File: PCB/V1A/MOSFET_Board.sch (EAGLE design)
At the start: 263 parts, among them IC301 7805T, IC302 7805T, J302 FAN_MOLEX4PIN, J303 FAN_MOLEX4PIN, Q201 SIRC10DP, Q202 SIRC10DP, Q203 BC817, Q204 BC817, Q205 SIRC10DP, Q206 SIRC10DP, Q207 BC817, Q208 BC807, Q209 BC817, Q210 BC807, Q211 IXTK102N65X2, Q212 IXTK102N65X2, Q401 BC807, Q402 BC807, Q403 BC807, Q404 BC807, Q405 BC807, Q406 BC807, Q407 BC807, Q408 BC807, Q409 BC807, Q410 BC807, Q411 BC807, Q412 BC807, Q413 BC807, Q414 BC807, U201 AD420, U202 AD420, U203 LT1014I, U204 LT1014I, U205 AD620, U206 AD620, U207 AD620, U208 AD620, U209 LTC1865L, U210 LTC1865L, U301 MAX743, U302 LP2985-3.1, U305 AD620, U306 LTC1865L, U307 LTC1865L, U401 HCPL-063N, U402 HCPL-063N, U403 HCPL-063N, U404 HCPL-063N, U405 HCPL-063N, U406 HCPL-063N, U407 HCPL-063N

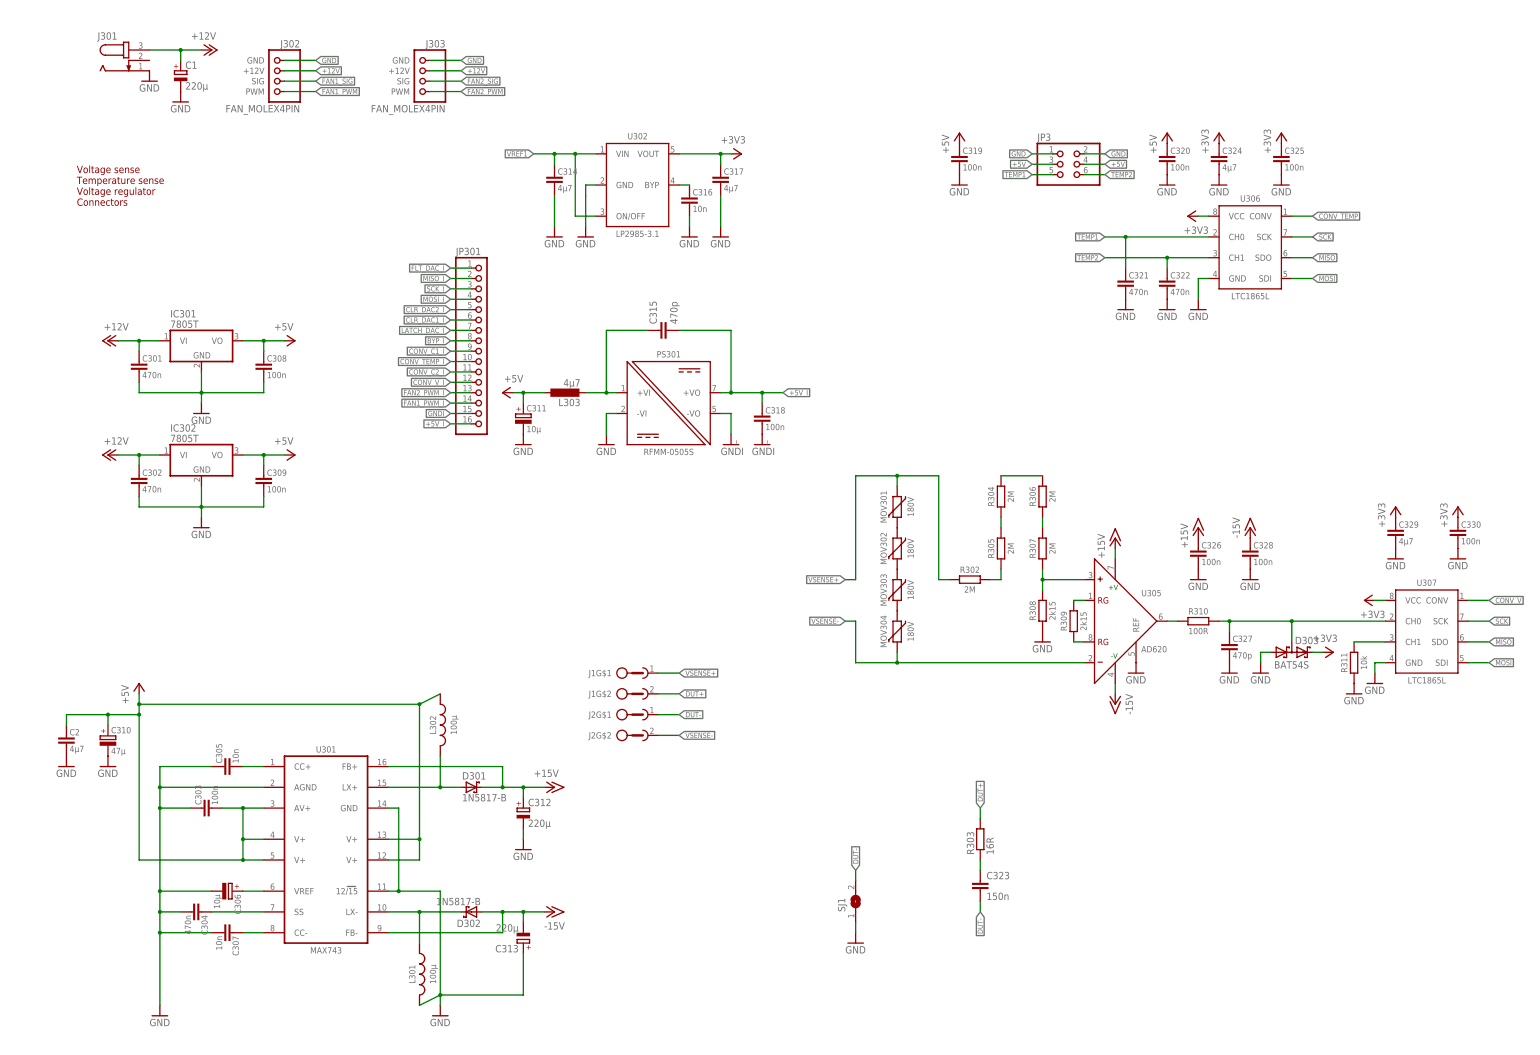
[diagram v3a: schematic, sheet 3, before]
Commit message: PCB layout & simulation
Added capacitance multiplier to +/-15V rails
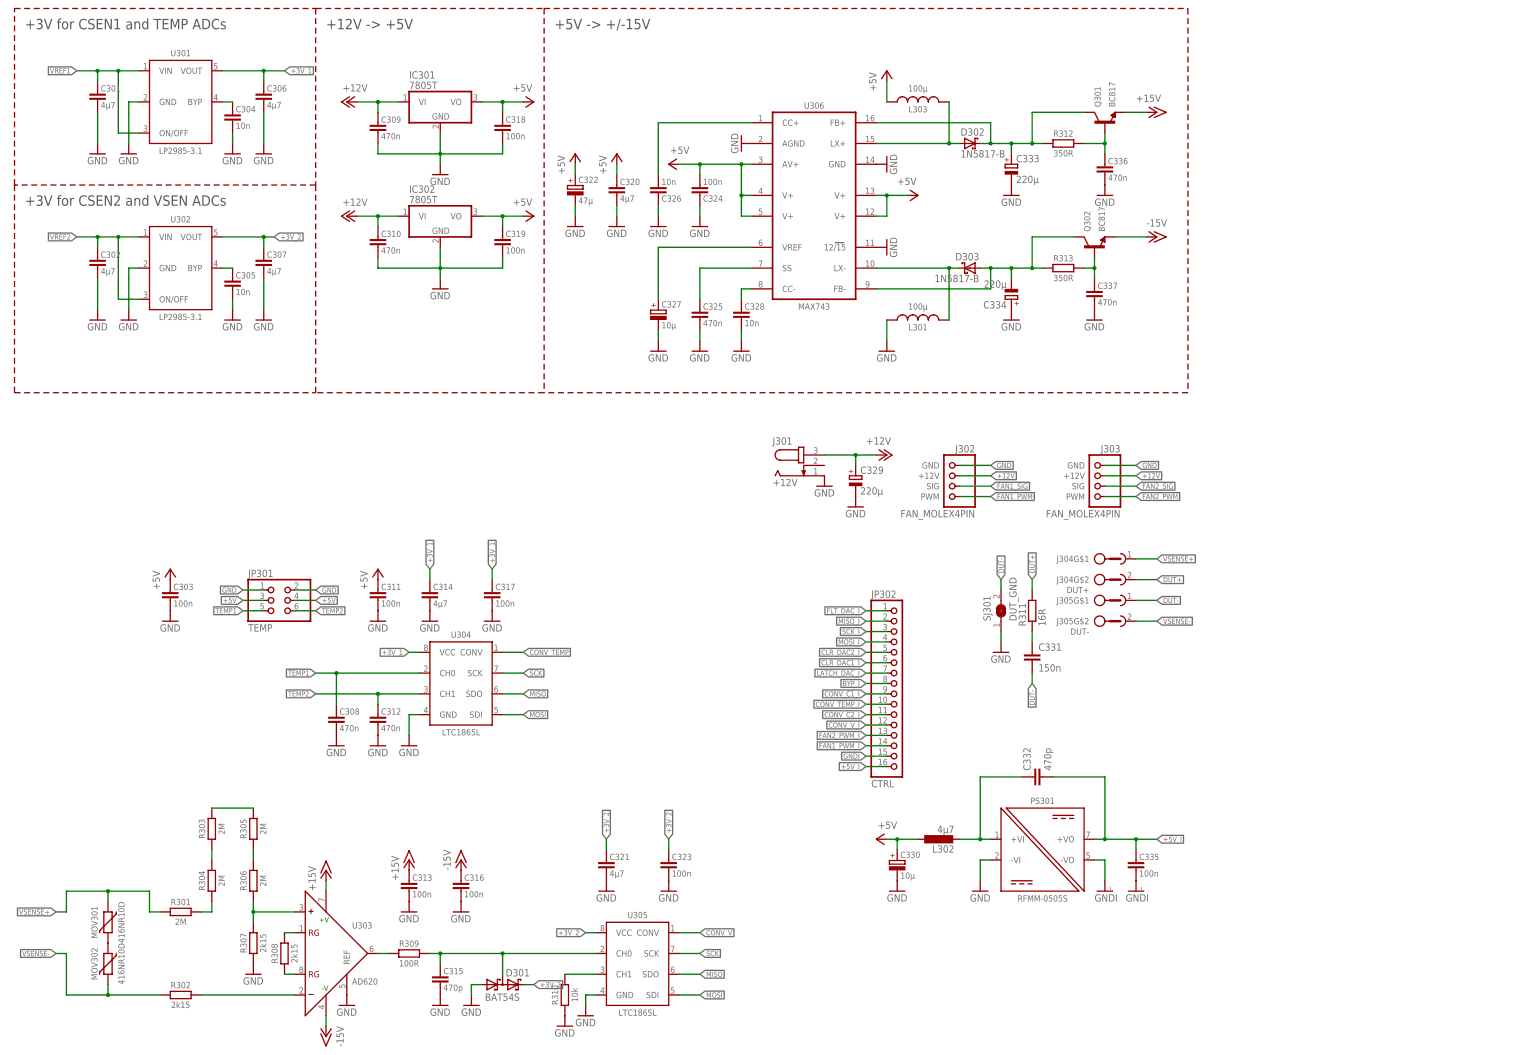
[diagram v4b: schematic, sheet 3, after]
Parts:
- removed C1: 220µ, rcl:CPOL-EUE3.5-10
- removed C2: 4µ7, passives:C-EU-3216
- removed J1, J2: (no value), mechanical:AMPHENOL_TERM-BLOCK_2
- removed JP3: (no value), pinhead:PINHD-2X3
- removed MOV303, MOV304: 180V, passives:MOV-3225
- removed SJ1: (no value), jumper:SJW
- removed U307: LTC1865L, ic:LTC1865L
- added C331: 150n, rcl:C-EU050-030X075
- added C332: 470p, rcl:C-EU075-032X103
- added C333, C334: 220µ, rcl:CPOL-EUE3.5-10
- added C335: 100n, passives:C-EU-1608
- added C336, C337: 470n, passives:C-EU-1608
- added J304: DUT+, mechanical:AMPHENOL_TERM-BLOCK_2
- added J305: DUT-, mechanical:AMPHENOL_TERM-BLOCK_2
- added JP302: CTRL, pinhead:PINHD-1X16
- added Q301, Q302: BC817, transistors:BC817
- added R301: 2M, passives:R-EU-3216
- added R312, R313: 350R, passives:R-EU-1608
- added SJ301: DUT_GND, jumper:SJW
- added U303: AD620, ic:AD620R-8
- added U304: LTC1865L, ic:LTC1865L
- C301, C302, C321: value 470n -> 4µ7; device passives:C-EU-1608 -> passives:C-EU-3216
- C304: value 470n -> 10n; device passives:C-EU-1608 -> passives:C-EU-2012
- C306: value 10µ -> 4µ7; device passives:CPOL-6032-C -> passives:C-EU-3216
- C307: value 10n -> 4µ7; device passives:C-EU-2012 -> passives:C-EU-3216
- C308, C309, C325: value 100n -> 470n
- C310: value 47µ -> 470n; device passives:CPOL-7343-DE -> passives:C-EU-1608
- C311: value 10µ -> 100n; device passives:CPOL-6032-C -> passives:C-EU-1608
- C312: value 220µ -> 470n; device rcl:CPOL-EUE3.5-10 -> passives:C-EU-1608
- C313: value 220µ -> 100n; device rcl:CPOL-EUE3.5-10 -> passives:C-EU-1608
- C315: device rcl:C-EU075-032X103 -> passives:C-EU-1608
- C316: value 10n -> 100n; device passives:C-EU-2012 -> passives:C-EU-1608
- C317, C324: value 4µ7 -> 100n; device passives:C-EU-3216 -> passives:C-EU-1608
- C320: value 100n -> 4µ7; device passives:C-EU-1608 -> passives:C-EU-3216
- C322: value 470n -> 47µ; device passives:C-EU-1608 -> passives:CPOL-7343-DE
- C323: value 150n -> 100n; device rcl:C-EU050-030X075 -> passives:C-EU-1608
- C326, C328: value 100n -> 10n; device passives:C-EU-1608 -> passives:C-EU-2012
- C327: value 470p -> 10µ; device passives:C-EU-1608 -> passives:CPOL-6032-C
- C329: value 4µ7 -> 220µ; device passives:C-EU-3216 -> rcl:CPOL-EUE3.5-10
- C330: value 100n -> 10µ; device passives:C-EU-1608 -> passives:CPOL-6032-C
- D301: value 1N5817-B -> BAT54S; device diode:1N5817-B -> diode:BAT54S
- D303: value BAT54S -> 1N5817-B; device diode:BAT54S -> diode:1N5817-B
- J301: value (none) -> +12V
- JP301: value (none) -> TEMP; device pinhead:PINHD-1X16 -> pinhead:PINHD-2X3
- L302: value 100µ -> 4µ7; device passives:L-EU_MSS1260 -> inductor-coilcraft:MSS7341
- L303: value 4µ7 -> 100µ; device inductor-coilcraft:MSS7341 -> passives:L-EU_MSS1260
- MOV301, MOV302: value 180V -> 416NR10D; device passives:MOV-3225 -> passives:MOV_9.5-DISK
- R302, R307: value 2M -> 2k15; device passives:R-EU-3216 -> passives:R-EU-2012
- R303: value 16R -> 2M; device rcl:R-EU_0204/7 -> passives:R-EU-3216
- R309: value 2k15 -> 100R; device passives:R-EU-2012 -> passives:R-EU-1608
- R310: value 100R -> 10k
- R311: value 10k -> 16R; device passives:R-EU-1608 -> rcl:R-EU_0204/7
- U301: value MAX743 -> LP2985-3.1; device ic:MAX743WE -> ic:LP2985-3.1
- U305: value AD620 -> LTC1865L; device ic:AD620R-8 -> ic:LTC1865L
- U306: value LTC1865L -> MAX743; device ic:LTC1865L -> ic:MAX743WE
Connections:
- new net +3V_1: C229.1, C231.1, C306.1, C314.1, C317.1, D201.C2, D202.C2, U209.VCC, U301.VOUT, U304.VCC
- new net +3V_2: C230.1, C232.1, C307.1, C321.1, C323.1, D203.C2, D204.C2, D301.C2, U210.VCC, U302.VOUT, U305.VCC
- new net N$62: C305.1, U302.BYP
- new net N$63: C336.1, Q301.B, R312.2
- new net N$64: C334.-, D303.A, Q302.C, R313.1, U306.FB-
- new net N$65: C337.1, Q302.B, R313.2
- net +12V: now also C309.1, C310.1, C329.+; no longer C1.+, C301.1, C302.1
- net +15V: now also C313.1, Q301.E, U303.+V; no longer C312.+, C326.1, D301.C, U301.FB+, U305.+V
- net +3V3: no longer C229.1, C230.1, C231.1, C232.1, C317.1, C324.1, C325.1, C329.1, C330.1, D201.C2, D202.C2, D203.C2, D204.C2, D303.C2, U209.VCC, U210.VCC, U302.VOUT, U306.VCC, U307.VCC
- net +5V: now also C303.1, C311.1, C318.1, C322.+, C324.2, C330.+, JP301.3, JP301.4, L302.2, L303.1, U306.AV+, U306.V+, U306.V+@1, U306.V+@2, U306.V+@3; no longer C2.1, C303.2, C308.1, C309.1, C310.+, C311.+, JP3.3, JP3.4, L302.1, L303.2, U301.AV+, U301.V+, U301.V+@1, U301.V+@2, U301.V+@3
- net +5V_I: now also C332.2, C335.1, JP302.16; no longer C315.2, C318.1, JP301.16
- net -15V: now also C316.1, Q302.E, U303.-V; no longer C313.-, C328.1, D302.A, U301.FB-, U305.-V
- net BYP_I: now also JP302.8; no longer JP301.8
- net CLR_DAC1_I: now also JP302.6; no longer JP301.6
- net CLR_DAC2_I: now also JP302.5; no longer JP301.5
- net CONV_C1_I: now also JP302.9; no longer JP301.9
- net CONV_C2_I: now also JP302.11; no longer JP301.11
- net CONV_TEMP: now also U304.CONV; no longer U306.CONV
- net CONV_TEMP_I: now also JP302.10; no longer JP301.10
- net CONV_V: now also U305.CONV; no longer U307.CONV
- net CONV_V_I: now also JP302.12; no longer JP301.12
- net DUT+: now also J304G$2.1, R311.2; no longer J1G$2.1, R303.2
- net DUT-: now also C331.2, J305G$1.1, SJ301.2; no longer C323.2, J2G$1.1, SJ1.2
- net FAN1_PWM_I: now also JP302.14; no longer JP301.14
- net FAN2_PWM_I: now also JP302.13; no longer JP301.13
- net FLT_DAC_I: now also JP302.1; no longer JP301.1
- net GND: now also C303.2, C305.2, C306.2, C310.2, C311.2, C312.2, C313.2, C315.2, C318.2, C322.-, C323.2, C324.1, C326.1, C327.-, C329.-, C330.-, C333.-, C334.+, C336.2, C337.2, D301.A1, JP301.1, JP301.2, R307.1, R310.1, SJ301.1, U303.REF, U304.GND, U305.GND, U306.12/15, U306.AGND; no longer C1.-, C2.2, C303.1, C305.1, C306.-, C310.-, C311.-, C312.-, C313.+, C322.2, C324.2, C326.2, C327.2, C329.2, C330.2, D303.A1, JP3.1, JP3.2, R308.1, R311.1, SJ1.1, U301.12/15, U301.AGND, U305.REF, U307.GND
- net GNDI: now also C335.2, JP302.15; no longer C318.2, JP301.15
- net LATCH_DAC_I: now also JP302.7; no longer JP301.7
- net MISO: now also U304.SDO, U305.SDO; no longer U306.SDO, U307.SDO
- net MISO_I: now also JP302.2; no longer JP301.2
- net MOSI: now also U304.SDI, U305.SDI; no longer U306.SDI, U307.SDI
- net MOSI_I: now also JP302.4; no longer JP301.4
- net N$10: now also C304.1, U301.BYP; no longer C316.1, U302.BYP
- net N$23: now also R309.1, U303.OUT; no longer R310.1, U305.OUT
- net N$24: now also R305.1, R306.2; no longer R306.1, R307.2
- net N$26: now also R303.2, R305.2; no longer R304.2, R306.2
- net N$27: now also R303.1, R304.2; no longer R304.1, R305.2
- net N$29: now also R306.1, R307.2, U303.+; no longer R307.1, R308.2, U305.+
- net N$30: now also C315.1, D301.C1A2, R309.2, U305.CH0; no longer C327.1, D303.C1A2, R310.2, U307.CH0
- net N$32: now also C333.+, D302.C, Q301.C, R312.1, U306.FB+; no longer MOV302.2, MOV303.1
- net N$33: now also R301.2, R304.1; no longer R302.2, R305.1
- net N$34: now also C328.1, U306.CC-; no longer C307.1, U301.CC-
- net N$35: now also C325.1, U306.SS; no longer C304.1, U301.SS
- net N$36: now also R302.2, U303.-; no longer MOV303.2, MOV304.1
- net N$37: now also C326.2, U306.CC+; no longer C305.2, U301.CC+
- net N$38: now also D302.A, L303.2, U306.LX+; no longer D301.A, L302.2, U301.LX+
- net N$39: now also D303.C, U306.LX-; no longer D302.C, U301.LX-
- net N$45: now also R310.2, U305.CH1; no longer R311.2, U307.CH1
- net N$60: now also C332.1, L302.1; no longer C315.1, L303.1
- net N$61: now also C331.1, R311.1; no longer C323.1, R303.1
- net RG1_H6: now also R308.2, U303.RG@1; no longer R309.2, U305.RG@1
- net RG2_H6: now also R308.1, U303.RG@2; no longer R309.1, U305.RG@2
- net SCK: now also U304.SCK, U305.SCK; no longer U306.SCK, U307.SCK
- net SCK_I: now also JP302.3; no longer JP301.3
- net TEMP1: now also C308.1, JP301.5, U304.CH0; no longer C321.1, JP3.5, U306.CH0
- net TEMP2: now also C312.1, JP301.6, U304.CH1; no longer C322.1, JP3.6, U306.CH1
- net VREF1: now also C301.1, U301.ON/OFF, U301.VIN; no longer C314.1, U302.ON/OFF, U302.VIN
- net VREF2: now also C302.1, U302.ON/OFF, U302.VIN
- net VREF_MAX743: now also C327.+, U306.VREF; no longer C306.+, U301.VREF
- net VSENSE+: now also J304G$1.1, R301.1; no longer J1G$1.1, R302.1
- net VSENSE-: now also J305G$2.1, MOV302.2, R302.1; no longer J2G$2.1, MOV304.2, U305.-
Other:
- note added: "+12V -> +5V"
- note added: "+3V for CSEN1 and TEMP ADCs"
- note added: "+3V for CSEN2 and VSEN ADCs"
- note added: "+5V -> +/-15V"
- note removed: "Voltage sense Temperature sense Voltage regulator Connectors"
- moved on the sheet: C301, C302, C303, C304, C305, C307, C308, C309, C314, C315, C316, C317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

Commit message: PCB layout
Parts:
- removed HS201, HS202: HEATSINK-LGA115X, mechanical:HEATSINK-LGA115X
- added C1, C2: 4µ7, passives:C-EU-3216
- added C3: 10n, passives:C-EU-2012
- added HS1: HEATSINK_LGA775, mechanical:HEATSINK_LGA775
- added HS2: HEATSINK_LGA115X, mechanical:HEATSINK_LGA115X
- added U1: LP2985-3.1, ic:LP2985-3.1
- JP301: device pinhead:PINHD-2X3 -> mechanical:HEAD_2X3_MALE
- JP302: device pinhead:PINHD-1X16 -> mechanical:HEAD_1X16_MALE
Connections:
- new net N$66: C3.1, U1.BYP
- net +3V3: now also C2.1, U1.VOUT
- net +5V: now also C1.1, U1.ON/OFF, U1.VIN
- net GND: now also C1.2, C2.2, C3.2, U1.GND
